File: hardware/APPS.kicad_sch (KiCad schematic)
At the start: 22 parts, among them SW1 SW_Push, U1 STM32L4P5RET6, Y1 8Mhz

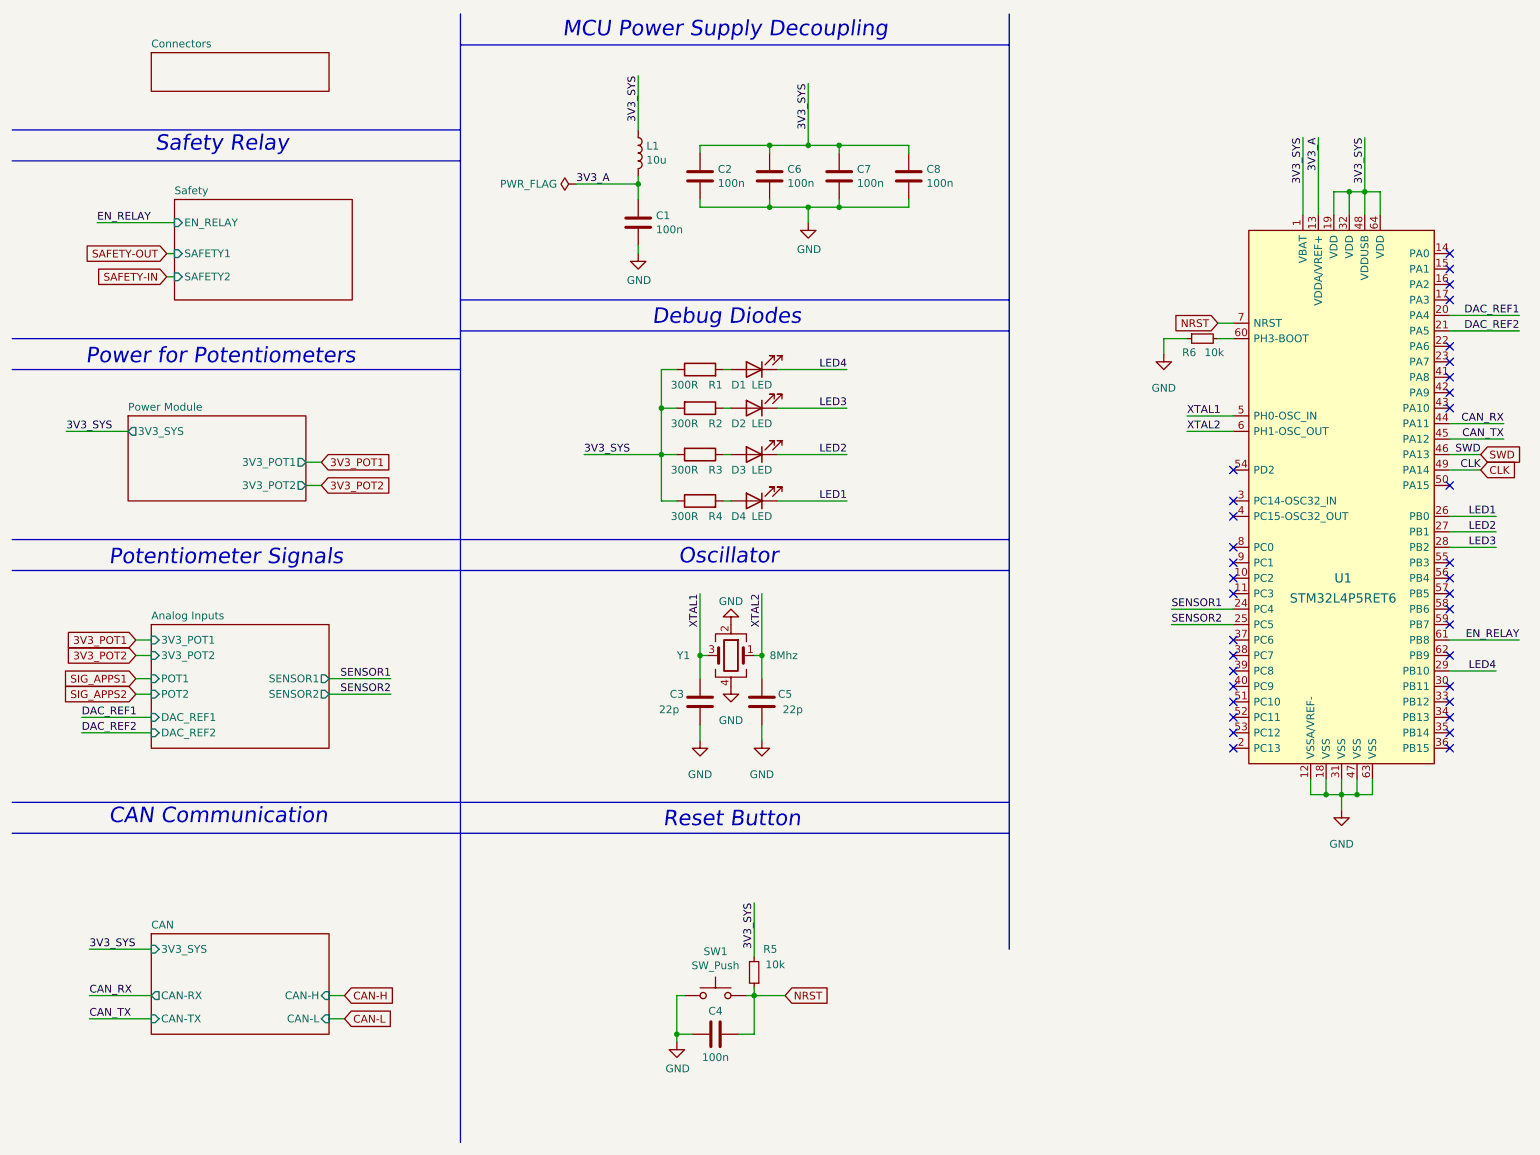
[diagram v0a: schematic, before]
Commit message: Add brake pressure sensors
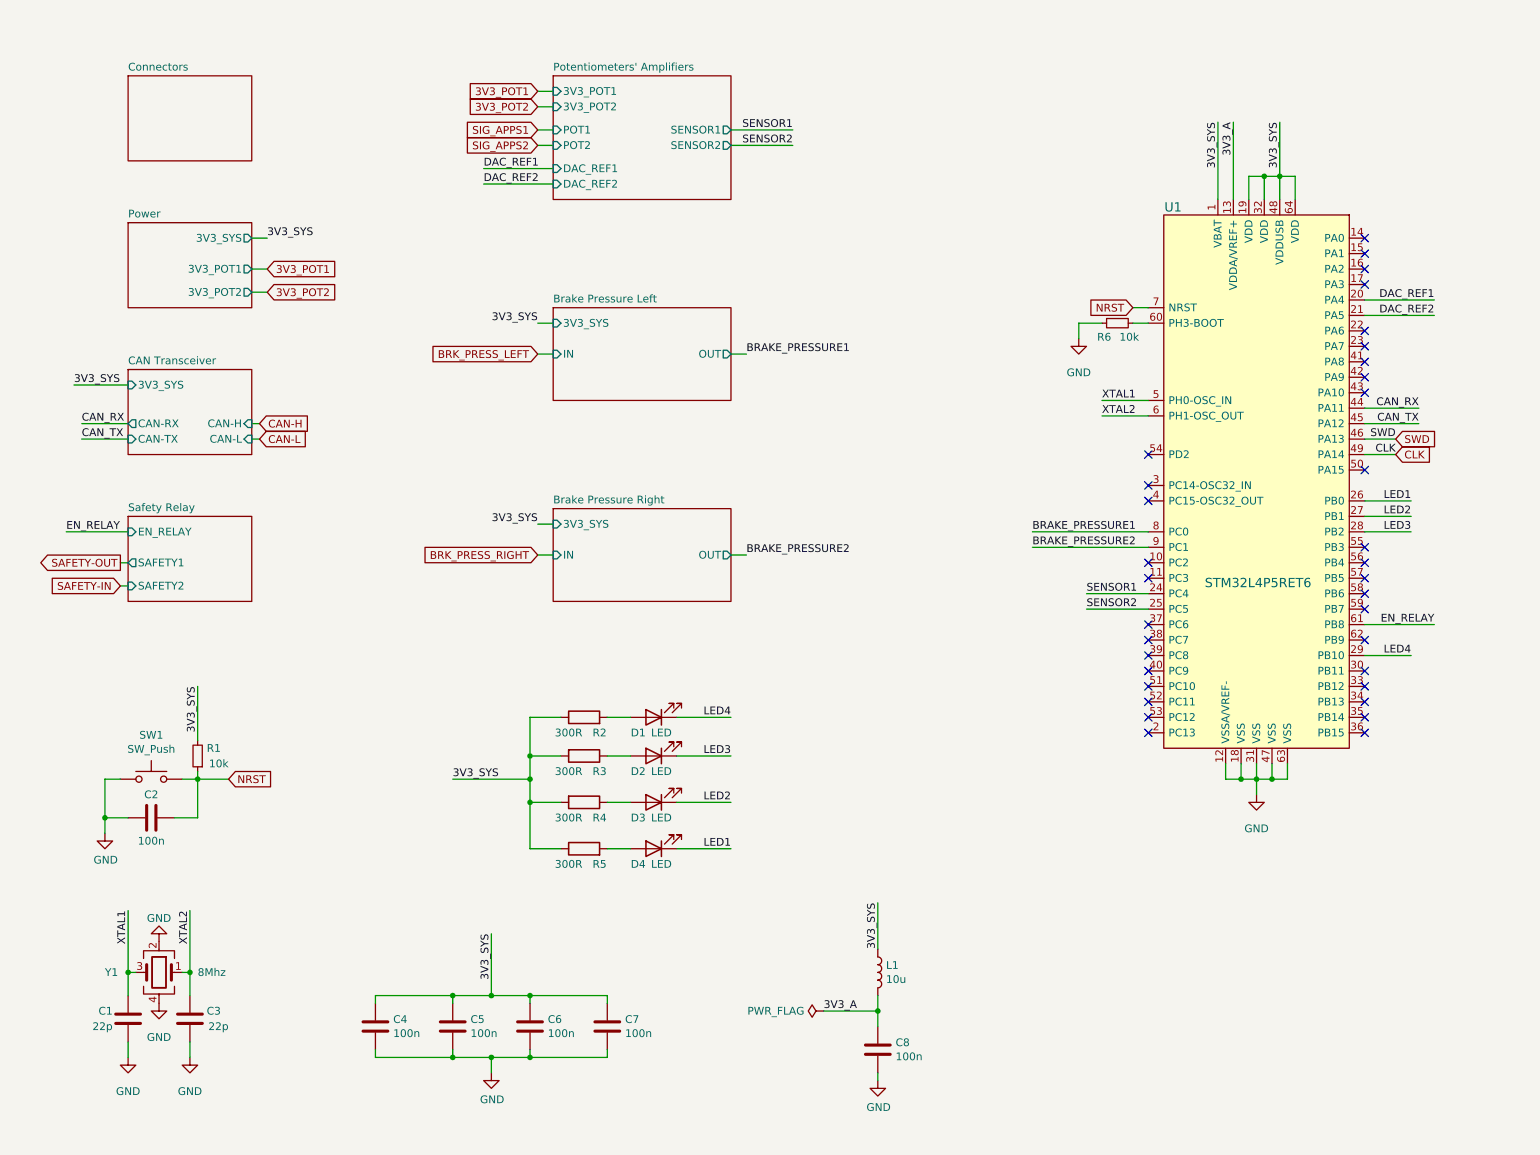
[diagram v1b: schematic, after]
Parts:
- L1: footprint Inductor_SMD:L_0805_2012Metric -> Inductor_SMD:L_0603_1608Metric_Pad1.05x0.95mm_HandSolder
- renumbered C3 to C1, C4 to C2, C5 to C3, C2 to C4, C6 to C5, C7 to C6, C8 to C7, C1 to C8, R5 to R1, R1 to R2, R2 to R3, R3 to R4, R4 to R5
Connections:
- net BRAKE_PRESSURE1: now reaches U1.8 (PC0)
- net BRAKE_PRESSURE2: now reaches U1.9 (PC1)
- no-connect marks 36 -> 34
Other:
- sheet Analog Inputs renamed Potentiometers' Amplifiers
- sheet CAN renamed CAN Transceiver
- sheet Power Module renamed Power
- sheet Safety renamed Safety Relay
- added sheet Brake Pressure Left (brake_pressure.kicad_sch)
- added sheet Brake Pressure Right (brake_pressure.kicad_sch)
- note removed: "CAN Communication"
- note removed: "Debug Diodes"
- note removed: "MCU Power Supply Decoupling"
- note removed: "Oscillator"
- note removed: "Potentiometer Signals"
- note removed: "Power for Potentiometers"
- note removed: "Reset Button"
- note removed: "Safety Relay"
- moved on the sheet: C1, C2, C3, C4, C5, C6, C7, C8, D1, D2, D3, D4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

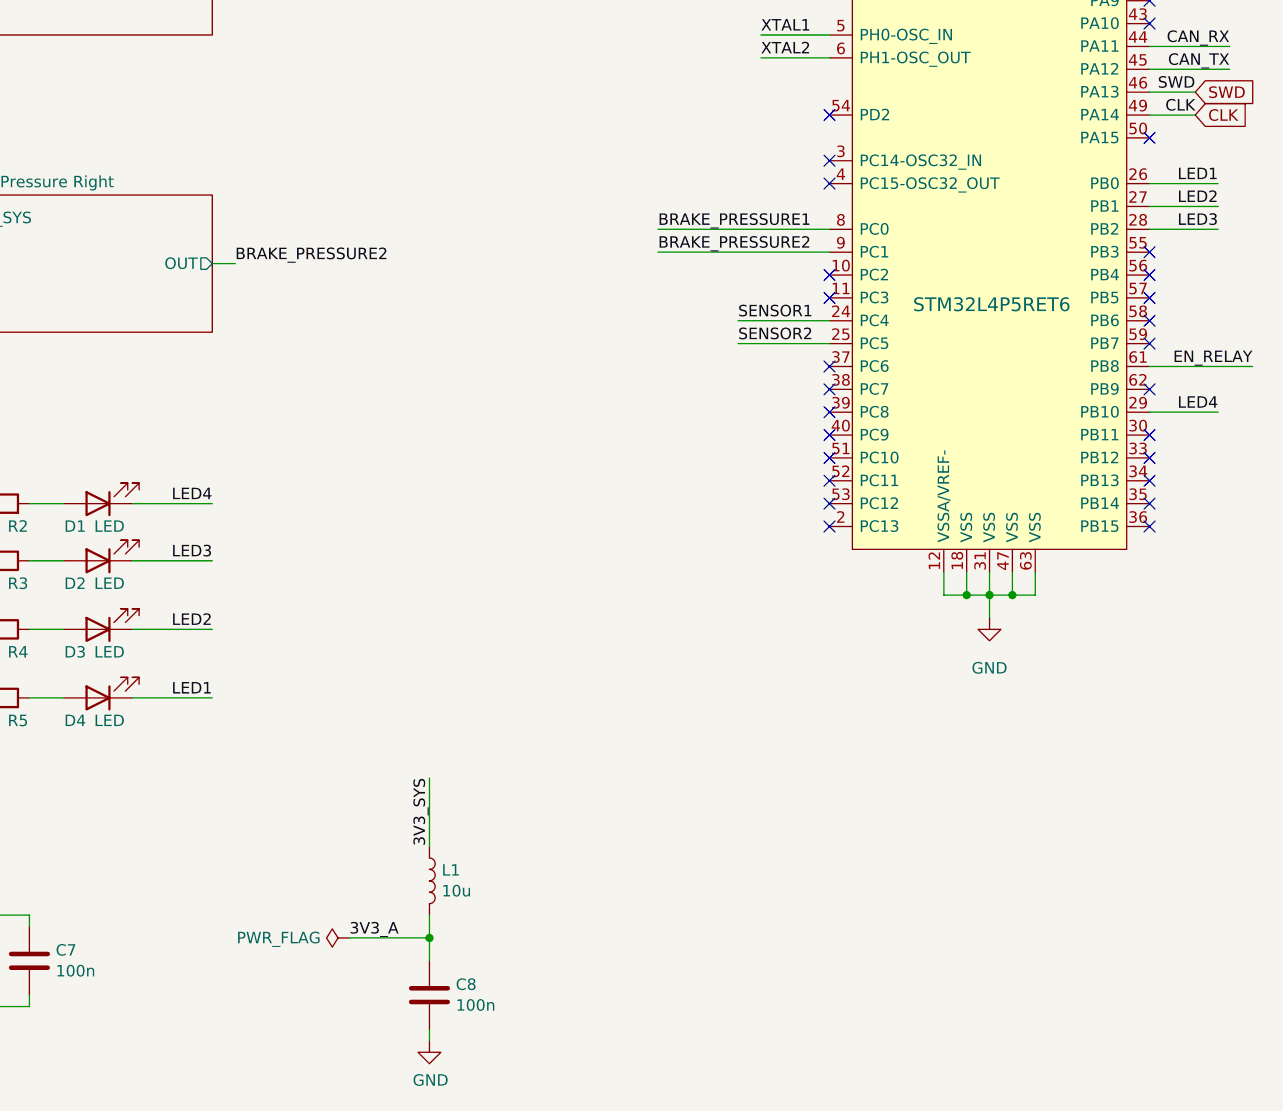
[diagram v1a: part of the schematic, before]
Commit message: Add 0R resistors to the brake pressure signals
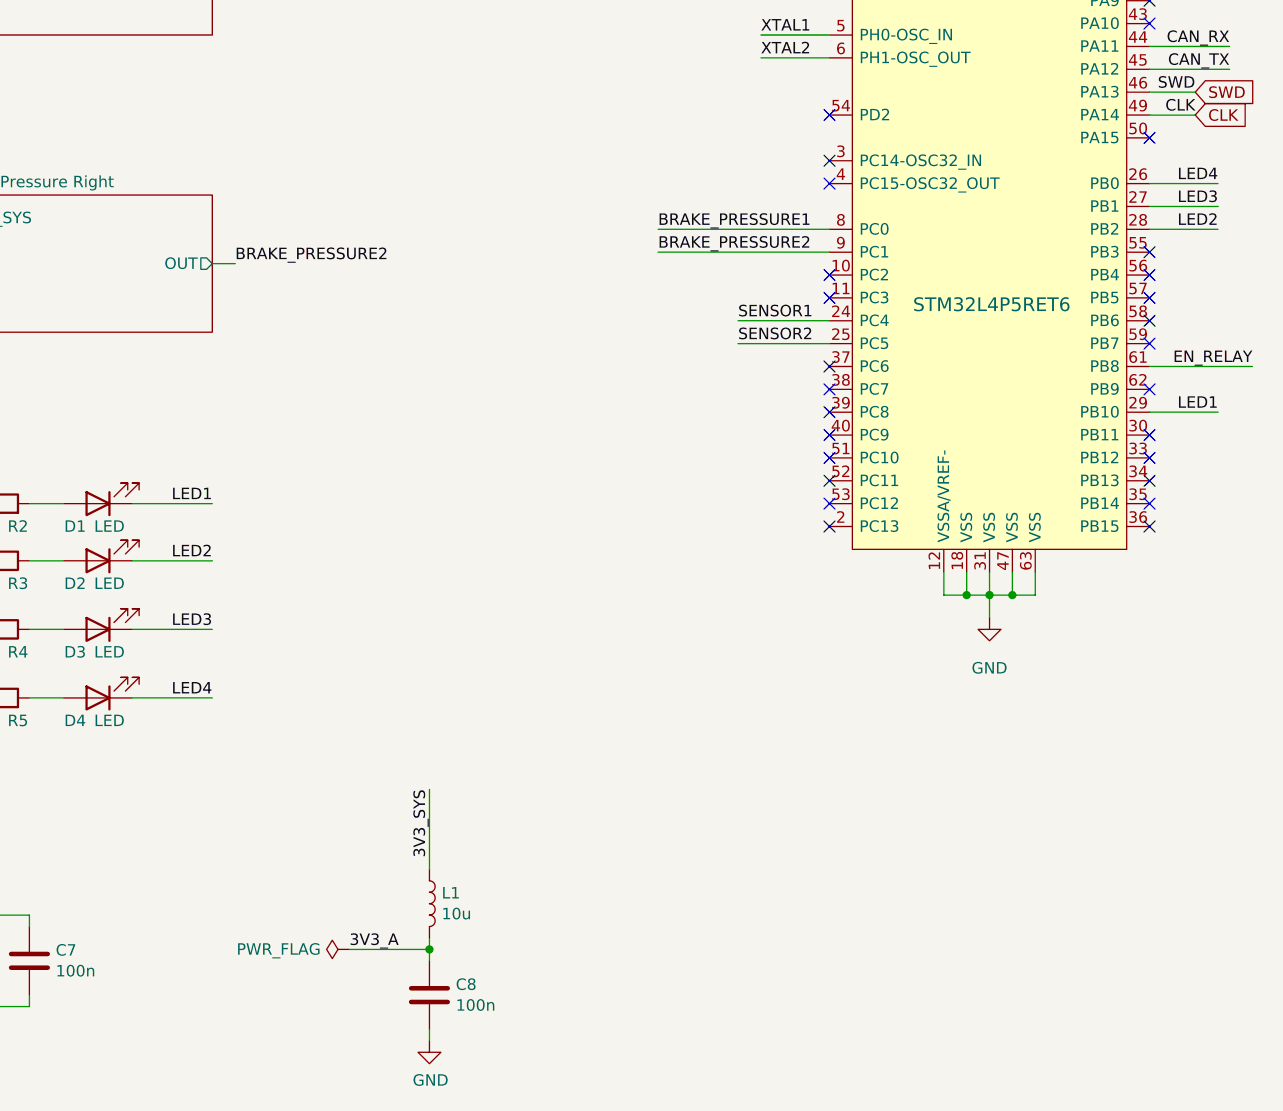
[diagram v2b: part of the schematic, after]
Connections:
- net LED1: now also D1.1 (K), U1.29 (PB10); no longer D4.1 (K), U1.26 (PB0)
- net LED2: now also D2.1 (K), U1.28 (PB2); no longer D3.1 (K), U1.27 (PB1)
- net LED3: now also D3.1 (K), U1.27 (PB1); no longer D2.1 (K), U1.28 (PB2)
- net LED4: now also D4.1 (K), U1.26 (PB0); no longer D1.1 (K), U1.29 (PB10)
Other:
- moved on the sheet: L1
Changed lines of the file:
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@@
   (title_block
     (title "Accelerator Pedal Position Sensor")
-    (date "2023-04-22")
+    (date "2023-05-02")
     (rev "2.0")
     (company "S. Sambor")
@@
   (junction (at 85.09 184.15) (diameter 0) (color 0 0 0 0)
   )
+  (junction (at 154.94 177.8) (diameter 0) (color 0 0 0 0)
+  )
   (junction (at 214.63 138.43) (diameter 0) (color 0 0 0 0)
   )
@@
   )
   (junction (at 85.09 173.99) (diameter 0) (color 0 0 0 0)
-  )
-  (junction (at 154.94 176.53) (diameter 0) (color 0 0 0 0)
   )
   (junction (at 97.79 142.24) (diameter 0) (color 0 0 0 0)
@@
     (stroke (width 0) (type default))
   )
-  (wire (pts (xy 154.94 179.07) (xy 154.94 176.53))
+  (wire (pts (xy 154.94 179.07) (xy 154.94 177.8))
     (stroke (width 0) (type default))
   )
@@
     (stroke (width 0) (type default))
   )
-  (wire (pts (xy 154.94 158.75) (xy 154.94 166.37))
+  (wire (pts (xy 154.94 160.02) (xy 154.94 168.91))
     (stroke (width 0) (type default))
   )
@@
     (stroke (width 0) (type default))
   )
+  (wire (pts (xy 154.94 176.53) (xy 154.94 177.8))
+    (stroke (width 0) (type default))
+  )
   (wire (pts (xy 154.94 186.69) (xy 154.94 187.96))
     (stroke (width 0) (type default))
@@
     (stroke (width 0) (type default))
   )
-  (wire (pts (xy 146.05 176.53) (xy 154.94 176.53))
+  (wire (pts (xy 146.05 177.8) (xy 154.94 177.8))
     (stroke (width 0) (type default))
   )
@@
     (stroke (width 0) (type default))
   )
-  (wire (pts (xy 154.94 176.53) (xy 154.94 173.99))
-    (stroke (width 0) (type default))
-  )
   (wire (pts (xy 110.49 184.15) (xy 97.79 184.15))
     (stroke (width 0) (type default))
   )
-  (label "LED3" (at 130.81 134.62 180) (fields_autoplaced)
+  (label "LED2" (at 130.81 134.62 180) (fields_autoplaced)
     (effects (font (size 1.27 1.27)) (justify right bottom))
   )
@@
     (effects (font (size 1.27 1.27)) (justify right bottom))
   )
-  (label "3V3_SYS" (at 154.94 158.75 270) (fields_autoplaced)
+  (label "3V3_SYS" (at 154.94 160.02 270) (fields_autoplaced)
     (effects (font (size 1.27 1.27)) (justify right bottom))
   )
@@
     (effects (font (size 1.27 1.27)) (justify left bottom))
   )
-  (label "LED3" (at 242.57 97.79 180) (fields_autoplaced)
+  (label "LED2" (at 242.57 97.79 180) (fields_autoplaced)
     (effects (font (size 1.27 1.27)) (justify right bottom))
   )
@@
     (effects (font (size 1.27 1.27)) (justify left bottom))
   )
-  (label "3V3_A" (at 146.05 176.53 0) (fields_autoplaced)
+  (label "3V3_A" (at 146.05 177.8 0) (fields_autoplaced)
     (effects (font (size 1.27 1.27)) (justify left bottom))
   )
@@
     (effects (font (size 1.27 1.27)) (justify left bottom))
   )
-  (label "LED2" (at 242.57 95.25 180) (fields_autoplaced)
+  (label "LED3" (at 242.57 95.25 180) (fields_autoplaced)
     (effects (font (size 1.27 1.27)) (justify right bottom))
   )
@@
     (effects (font (size 1.27 1.27)) (justify left bottom))
   )
-  (label "LED2" (at 130.81 142.24 180) (fields_autoplaced)
+  (label "LED3" (at 130.81 142.24 180) (fields_autoplaced)
     (effects (font (size 1.27 1.27)) (justify right bottom))
   )
@@
     (effects (font (size 1.27 1.27)) (justify right bottom))
   )
-  (label "LED1" (at 130.81 149.86 180) (fields_autoplaced)
+  (label "LED4" (at 130.81 149.86 180) (fields_autoplaced)
     (effects (font (size 1.27 1.27)) (justify right bottom))
   )
@@
     (effects (font (size 1.27 1.27)) (justify right bottom))
   )
-  (label "LED4" (at 242.57 118.11 180) (fields_autoplaced)
-    (effects (font (size 1.27 1.27)) (justify right bottom))
-  )
-  (label "LED4" (at 130.81 128.27 180) (fields_autoplaced)
+  (label "LED1" (at 242.57 118.11 180) (fields_autoplaced)
+    (effects (font (size 1.27 1.27)) (justify right bottom))
+  )
+  (label "LED1" (at 130.81 128.27 180) (fields_autoplaced)
     (effects (font (size 1.27 1.27)) (justify right bottom))
   )
@@
     (effects (font (size 1.27 1.27)) (justify left bottom))
   )
-  (label "LED1" (at 242.57 92.71 180) (fields_autoplaced)
+  (label "LED4" (at 242.57 92.71 180) (fields_autoplaced)
     (effects (font (size 1.27 1.27)) (justify right bottom))
   )
@@
     )
   )
-  (symbol (lib_id "Device:L") (at 154.94 170.18 0) (unit 1)
-    (in_bom yes) (on_board yes) (dnp no)
-    (property "Reference" "L1" (at 156.2862 169.0116 0)
-      (effects (font (size 1.27 1.27)) (justify left))
-    )
-    (property "Value" "10u" (at 156.2862 171.323 0)
-      (effects (font (size 1.27 1.27)) (justify left))
-    )
-    (property "Footprint" "Inductor_SMD:L_0603_1608Metric_Pad1.05x0.95mm_HandSolder" (at 154.94 170.18 0)
-      (effects (font (size 1.27 1.27)) hide)
-    )
-    (property "Datasheet" "~" (at 154.94 170.18 0)
+  (symbol (lib_id "Device:L") (at 154.94 172.72 0) (unit 1)
+    (in_bom yes) (on_board yes) (dnp no)
+    (property "Reference" "L1" (at 156.2862 171.5516 0)
+      (effects (font (size 1.27 1.27)) (justify left))
+    )
+    (property "Value" "10u" (at 156.2862 173.863 0)
+      (effects (font (size 1.27 1.27)) (justify left))
+    )
+    (property "Footprint" "Inductor_SMD:L_0603_1608Metric_Pad1.05x0.95mm_HandSolder" (at 154.94 172.72 0)
+      (effects (font (size 1.27 1.27)) hide)
+    )
+    (property "Datasheet" "~" (at 154.94 172.72 0)
       (effects (font (size 1.27 1.27)) hide)
     )
@@
     )
   )
-  (symbol (lib_id "power:PWR_FLAG") (at 146.05 176.53 90) (unit 1)
+  (symbol (lib_id "power:PWR_FLAG") (at 146.05 177.8 90) (unit 1)
     (in_bom yes) (on_board yes) (dnp no) (fields_autoplaced)
-    (property "Reference" "#FLG01" (at 144.145 176.53 0)
-      (effects (font (size 1.27 1.27)) hide)
-    )
-    (property "Value" "PWR_FLAG" (at 142.875 176.5299 90)
-      (effects (font (size 1.27 1.27)) (justify left))
-    )
-    (property "Footprint" "" (at 146.05 176.53 0)
-      (effects (font (size 1.27 1.27)) hide)
-    )
-    (property "Datasheet" "~" (at 146.05 176.53 0)
-      (effects (font (size 1.27 1.27)) hide)
-    )
+    (property "Reference" "#FLG01" (at 144.145 177.8 0)
+      (effects (font (size 1.27 1.27)) hide)
+    )
+    (property "Value" "PWR_FLAG" (at 142.875 177.7999 90)
+      (effects (font (size 1.27 1.27)) (justify left))
+    )
+    (property "Footprint" "" (at 146.05 177.8 0)
+      (effects (font (size 1.27 1.27)) hide)
+    )
+    (property "Datasheet" "~" (at 146.05 177.8 0)
+      (effects (font (size 1.27 1.27)) hide)
+    )
